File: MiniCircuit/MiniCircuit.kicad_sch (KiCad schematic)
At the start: 45 parts, among them J1 Conn_02x16_Odd_Even, J2 Conn_02x05_Odd_Even, SW1 SW_DIP_x08, U1 LM6172, U2 OPA2277, U3 MCP3008, U4 MCP4921, U5 CD4066BE, U6 CD4066BE, U7 CD4066BE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

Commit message: Verified PCB, near final testing
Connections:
- net ADC_CSbar: now also J1.22 (Pin_22); no longer J1.26 (Pin_26)
- net CLK: now also J1.18 (Pin_18); no longer J1.22 (Pin_22)
- net Control1: now also J1.9 (Pin_9); no longer J1.5 (Pin_5)
- net Control10A: now also J1.17 (Pin_17); no longer J1.13 (Pin_13)
- net Control10B: now also J1.13 (Pin_13); no longer J1.9 (Pin_9)
- net Control7: now also J1.5 (Pin_5); no longer J1.1 (Pin_1)
- net Control8: now also J1.7 (Pin_7); no longer J1.3 (Pin_3)
- net Control9A: now also J1.11 (Pin_11); no longer J1.7 (Pin_7)
- net Control9B: now also J1.15 (Pin_15); no longer J1.11 (Pin_11)
- net ControlAF_1A: now also J1.23 (Pin_23); no longer J1.19 (Pin_19)
- net ControlAF_1B: now also J1.19 (Pin_19); no longer J1.15 (Pin_15)
- net ControlAF_2A: now also J1.21 (Pin_21); no longer J1.17 (Pin_17)
- net ControlAF_2B: now also J1.25 (Pin_25); no longer J1.21 (Pin_21)
- net ControlAF_3A: now also J1.27 (Pin_27); no longer J1.23 (Pin_23)
- net ControlAF_3B: now also J1.28 (Pin_28); no longer J1.27 (Pin_27)
- net ControlAF_4A: now also J1.26 (Pin_26); no longer J1.29 (Pin_29)
- net ControlAF_4B: now also J1.29 (Pin_29); no longer J1.25 (Pin_25)
- net DAC_CSbar: now also J1.1 (Pin_1); no longer J1.4 (Pin_4)
- net Din: now also J1.24 (Pin_24); no longer J1.28 (Pin_28)
- net Dout: now also J1.20 (Pin_20); no longer J1.24 (Pin_24)
- net LDACbar: now also J1.3 (Pin_3); no longer J1.2 (Pin_2)
- net SCK: now also J1.2 (Pin_2); no longer J1.6 (Pin_6)
- net SDI: now also J1.4 (Pin_4); no longer J1.8 (Pin_8)

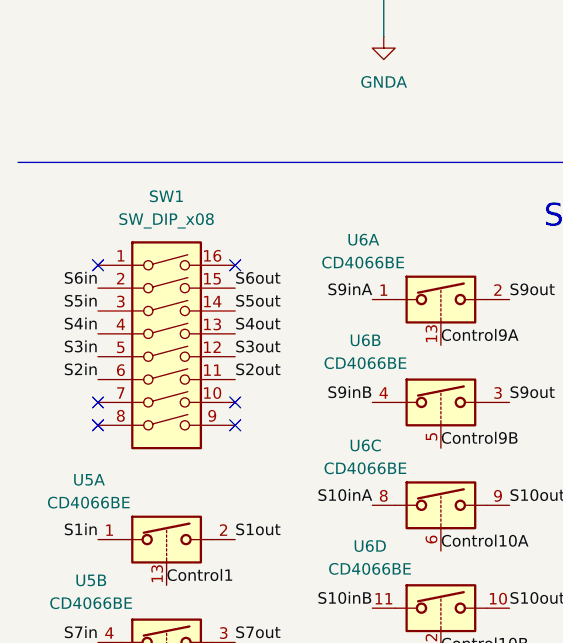
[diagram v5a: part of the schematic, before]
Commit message: Modified as per final component footprints
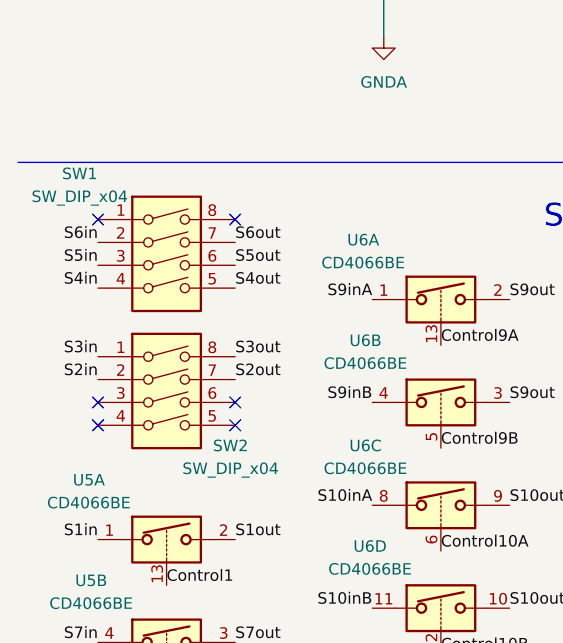
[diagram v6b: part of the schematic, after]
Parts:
- removed SW1: SW_DIP_x08, Button_Switch_THT:SW_DIP_SPSTx08_Slide_9.78x22.5mm_W7.62mm_P2.54mm, symbol Switch:SW_DIP_x08
- added SW1, SW2: SW_DIP_x04, Button_Switch_THT:SW_DIP_SPSTx04_Slide_9.78x12.34mm_W7.62mm_P2.54mm, symbol Switch:SW_DIP_x04
- FB1, FB2, FB3, FB4, FB5: footprint Inductor_SMD:L_1206_3216Metric_Pad1.22x1.90mm_HandSolder -> Inductor_SMD:L_0805_2012Metric_Pad1.15x1.40mm_HandSolder
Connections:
- net Driver_FB: now also SW1.2, SW1.3, SW1.4, SW2.1, SW2.2
- net S2out: now also SW2.7
- net S3out: now also SW2.8
- net S4out: now also SW1.5
- net S5out: now also SW1.6
- net S6out: now also SW1.7

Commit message: Added final touches
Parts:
- added H1, H2, H3: MountingHole, MountingHole:MountingHole_3mm, symbol Mechanical:MountingHole
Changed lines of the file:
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@@
+	)
+	(symbol
+		(lib_id "Mechanical:MountingHole")
+		(at 167.64 87.63 0)
+		(unit 1)
+		(exclude_from_sim yes)
+		(in_bom no)
+		(on_board yes)
+		(dnp no)
+		(fields_autoplaced yes)
+		(property "Reference" "H1"
+			(at 170.18 86.3599 0)
+			(effects
+				(font
+					(size 1.27 1.27)
+				)
+				(justify left)
+			)
+		)
+		(property "Value" "MountingHole"
+			(at 170.18 88.8999 0)
+			(effects
+				(font
+					(size 1.27 1.27)
+				)
+				(justify left)
+			)
+		)
+		(property "Footprint" "MountingHole:MountingHole_3mm"
+			(at 167.64 87.63 0)
+			(effects
+				(font
+					(size 1.27 1.27)
+				)
+				(hide yes)
+			)
+		)
+		(property "Datasheet" "~"
+			(at 167.64 87.63 0)
+			(effects
+				(font
+					(size 1.27 1.27)
+				)
+				(hide yes)
+			)
+		)
+		(property "Description" "Mounting Hole without connection"
+			(at 167.64 87.63 0)
+			(effects
+				(font
+					(size 1.27 1.27)
+				)
+				(hide yes)
+			)
+		)
+		(instances
+			(project "MiniCircuit"
+				(path "/ed26f7ee-1e82-4f03-9269-cad330ded895"
+					(reference "H1")
+					(unit 1)
+				)
+			)
+		)
 	)
 	(symbol
@@
 					(unit 1)
 				)
+			)
+		)
+	)
+	(symbol
+		(lib_id "Mechanical:MountingHole")
+		(at 208.28 87.63 0)
+		(unit 1)
+		(exclude_from_sim yes)
+		(in_bom no)
+		(on_board yes)
+		(dnp no)
+		(fields_autoplaced yes)
+		(property "Reference" "H3"
+			(at 210.82 86.3599 0)
+			(effects
+				(font
+					(size 1.27 1.27)
+				)
+				(justify left)
+			)
+		)
+		(property "Value" "MountingHole"
+			(at 210.82 88.8999 0)
+			(effects
+				(font
+					(size 1.27 1.27)
+				)
+				(justify left)
+			)
+		)
+		(property "Footprint" "MountingHole:MountingHole_3mm"
+			(at 208.28 87.63 0)
+			(effects
+				(font
+					(size 1.27 1.27)
+				)
+				(hide yes)
+			)
+		)
+		(property "Datasheet" "~"
+			(at 208.28 87.63 0)
+			(effects
+				(font
+					(size 1.27 1.27)
+				)
+				(hide yes)
+			)
+		)
+		(property "Description" "Mounting Hole without connection"
+			(at 208.28 87.63 0)
+			(effects
+				(font
+					(size 1.27 1.27)
+				)
+				(hide yes)
+			)
+		)
+		(instances
+			(project "MiniCircuit"
+				(path "/ed26f7ee-1e82-4f03-9269-cad330ded895"
+					(reference "H3")
+					(unit 1)
+				)
+			)
+		)
+	)
+	(symbol
+		(lib_id "Mechanical:MountingHole")
+		(at 189.23 87.63 0)
+		(unit 1)
+		(exclude_from_sim yes)
+		(in_bom no)
+		(on_board yes)
+		(dnp no)
+		(fields_autoplaced yes)
+		(property "Reference" "H2"
+			(at 191.77 86.3599 0)
+			(effects
+				(font
+					(size 1.27 1.27)
+				)
+				(justify left)
+			)
+		)
+		(property "Value" "MountingHole"
+			(at 191.77 88.8999 0)
+			(effects
+				(font
+					(size 1.27 1.27)
+				)
+				(justify left)
+			)
+		)
+		(property "Footprint" "MountingHole:MountingHole_3mm"
+			(at 189.23 87.63 0)
+			(effects
+				(font
+					(size 1.27 1.27)
+				)
+				(hide yes)
+			)
+		)
+		(property "Datasheet" "~"
+			(at 189.23 87.63 0)
+			(effects
+				(font
+					(size 1.27 1.27)
+				)
+				(hide yes)
+			)
+		)
+		(property "Description" "Mounting Hole without connection"
+			(at 189.23 87.63 0)
+			(effects
+				(font
+					(size 1.27 1.27)
+				)
+				(hide yes)
+			)
+		)
+		(instances
+			(project "MiniCircuit"
+				(path "/ed26f7ee-1e82-4f03-9269-cad330ded895"
+					(reference "H2")
+					(unit 1)
+				)
